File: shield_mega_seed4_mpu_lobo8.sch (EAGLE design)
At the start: 37 parts, among them U1 GY-521MPU6050

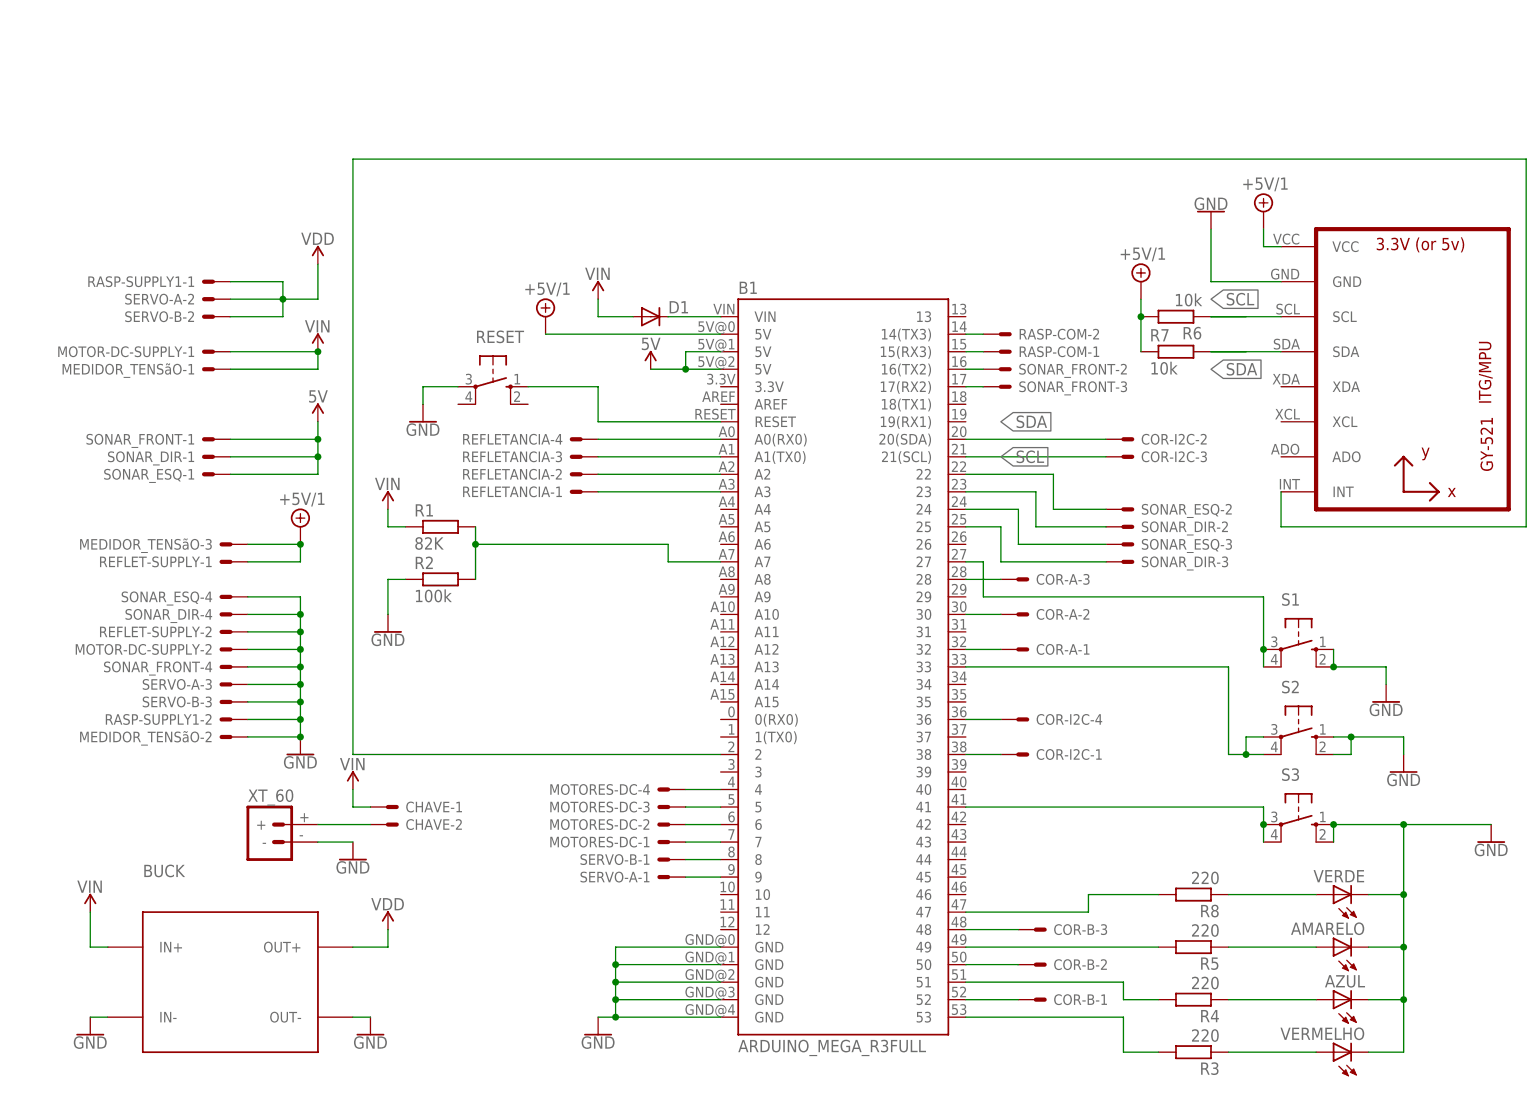
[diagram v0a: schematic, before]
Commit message: Adição de módulo bluetooth; Remoção do buck; Remoção de conector XT-60; Remoção de conector da chave;
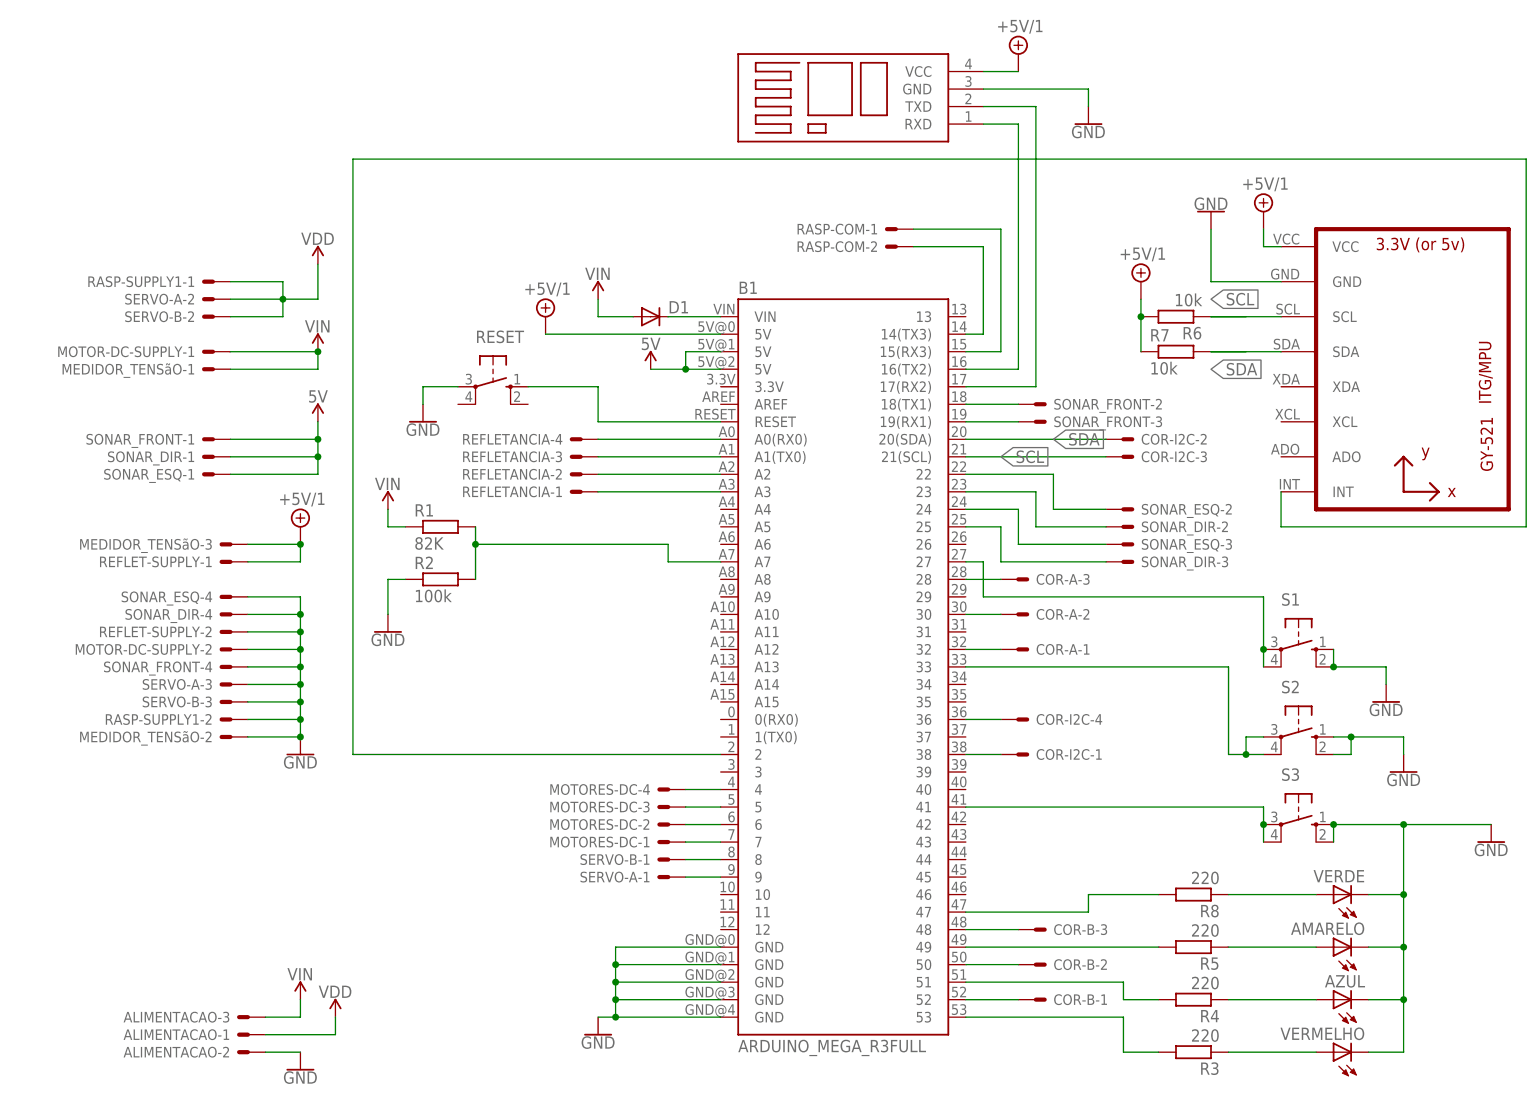
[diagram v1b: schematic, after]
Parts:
- removed BUCK: DC-DC-STEP-DOWN-LM2596, 1484249208697-powermodules:DC-DC-STEP-DOWN-LM2596
- removed CHAVE: 22-23-2021, con-molex:22-23-2021
- removed XT_60: (no value), Robotica-IFRN-SC-conectores:BATTERY_CONNXT60
- added ALIMENTACAO: 22-23-2031, con-molex:22-23-2031
- added B2: (no value), Bluetooth:BLUETOOTH
- R1, R2: device rcl:R-EU_0207/12 -> rcl:R-EU_0204/7
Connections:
- new net N$43: B1.17(RX2), B2.TXD
- net +5V/1: now also B2.VCC
- net GND: now also ALIMENTACAO-2.S, B2.GND; no longer BUCK.IN-, BUCK.OUT-, XT_60.-
- net N$11: now also B1.19(RX1), SONAR_FRONT-3.S; no longer B1.16(TX2), SONAR_FRONT-2.S
- net N$12: now also B1.18(TX1), SONAR_FRONT-2.S; no longer B1.17(RX2), SONAR_FRONT-3.S
- net N$13: now also B1.16(TX2), B2.RXD; no longer CHAVE-2.S, XT_60.+
- net VDD: now also ALIMENTACAO-1.S; no longer BUCK.OUT+
- net VIN: now also ALIMENTACAO-3.S; no longer BUCK.IN+, CHAVE-1.S
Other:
- moved on the sheet: RASP-COM-1, RASP-COM-2, SONAR_FRONT-2, SONAR_FRONT-3

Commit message: Remoção do conector do multímetro; remoção do conector de alimentação do sensor de refletância; remoção do conector de alimentação do motor;
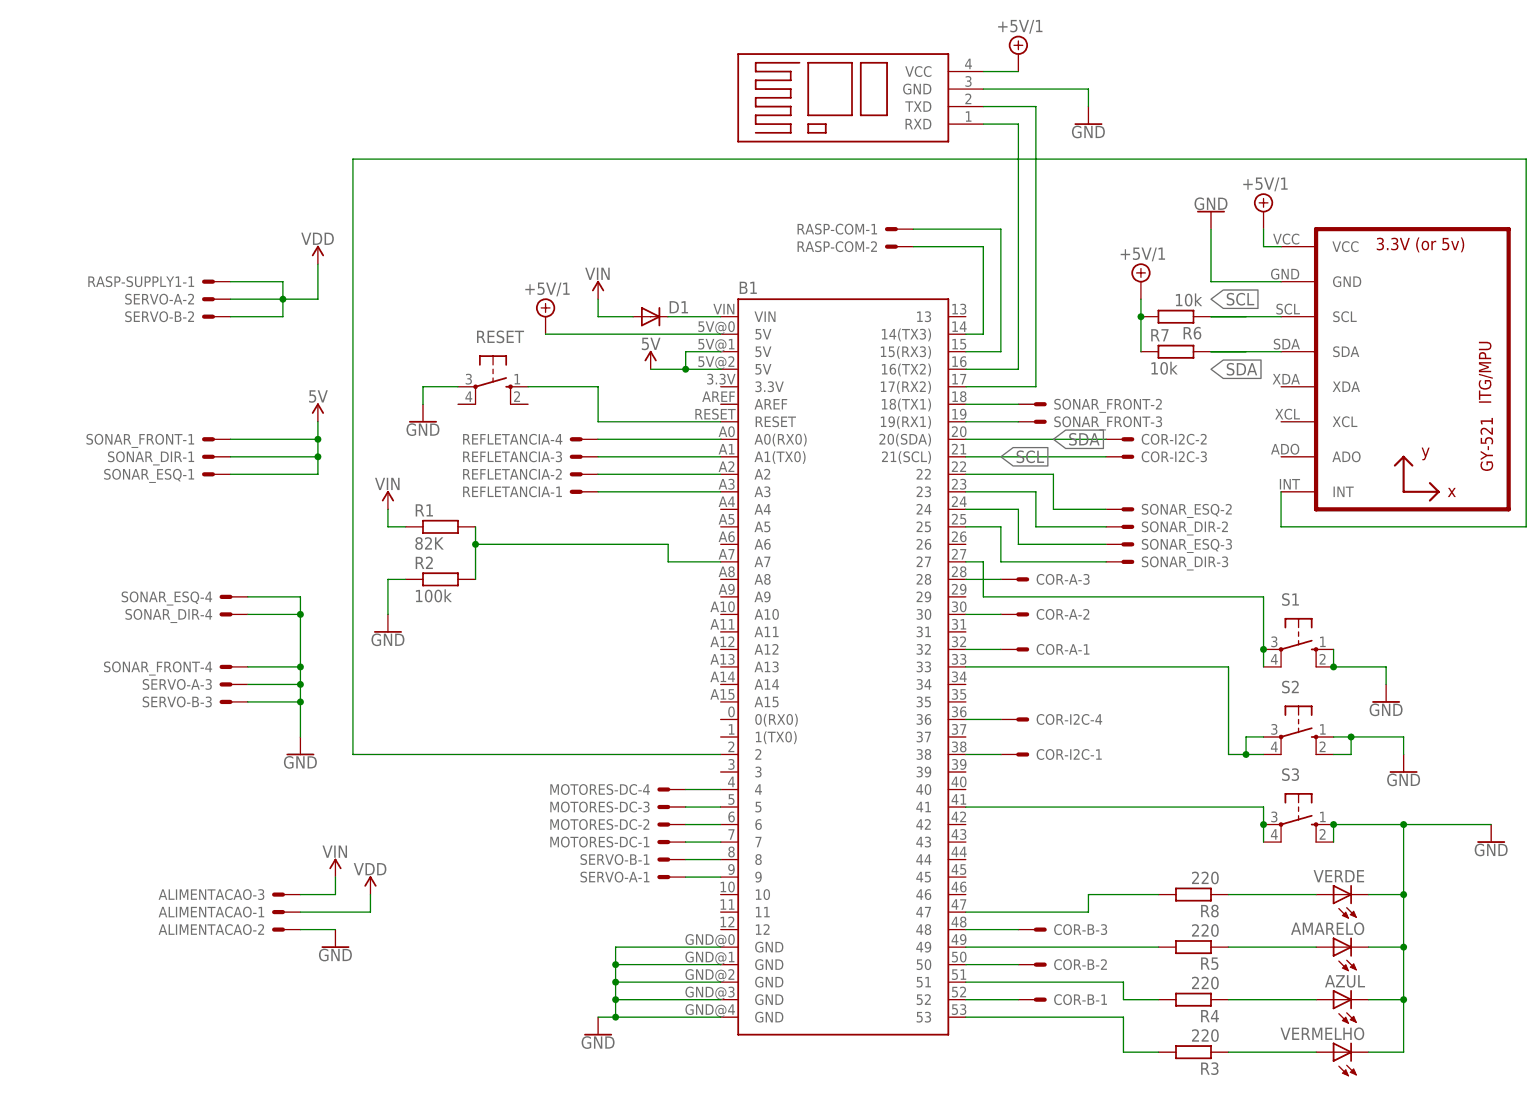
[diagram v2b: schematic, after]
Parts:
- removed MEDIDOR_TENSãO: 22-23-2031, con-molex:22-23-2031
- removed MOTOR-DC-SUPPLY, REFLET-SUPPLY: 22-23-2021, con-molex:22-23-2021
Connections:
- net +5V/1: no longer MEDIDOR_TENSãO-3.S, REFLET-SUPPLY-1.S
- net GND: no longer MEDIDOR_TENSãO-2.S, MOTOR-DC-SUPPLY-2.S, RASP-SUPPLY1-2.S, REFLET-SUPPLY-2.S
- net VIN: no longer MEDIDOR_TENSãO-1.S, MOTOR-DC-SUPPLY-1.S
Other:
- moved on the sheet: ALIMENTACAO-1, ALIMENTACAO-2, ALIMENTACAO-3
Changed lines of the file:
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@@
 </classes>
 <parts>
-<part name="B1" library="SparkFun-Boards3" deviceset="ARDUINO_MEGA_R3" device="FULL"/>
+<part name="B1" library="SparkFun-Boards3" deviceset="ARDUINO_MEGA_R3" device="FULL" value=""/>
 <part name="SUPPLY1" library="SparkFun-PowerSymbols" deviceset="VIN" device=""/>
 <part name="SUPPLY2" library="SparkFun-PowerSymbols" deviceset="VIN" device=""/>
@@
 <part name="SERVO-B" library="con-molex" deviceset="22-23-2031" device="" value=""/>
 <part name="MOTORES-DC" library="con-molex" deviceset="22-23-2041" device="" value=""/>
-<part name="MOTOR-DC-SUPPLY" library="con-molex" deviceset="22-23-2021" device="" value=""/>
 <part name="SUPPLY6" library="SparkFun-PowerSymbols" deviceset="VDD" device=""/>
 <part name="SUPPLY7" library="SparkFun-PowerSymbols" deviceset="VDD" device=""/>
@@
 <part name="RESET" library="switch-omron" deviceset="10-XX" device=""/>
 <part name="GND11" library="SparkFun-PowerSymbols" deviceset="GND" device=""/>
-<part name="MEDIDOR_TENSãO" library="con-molex" deviceset="22-23-2031" device="" value=""/>
-<part name="REFLET-SUPPLY" library="con-molex" deviceset="22-23-2021" device="" value=""/>
-<part name="SUPPLY4" library="SparkFun-PowerSymbols" deviceset="VIN" device=""/>
 <part name="SONAR_DIR" library="con-molex" deviceset="22-23-2041" device="" value=""/>
 <part name="SUPPLY9" library="SparkFun-PowerSymbols" deviceset="5V" device=""/>
 <part name="SONAR_ESQ" library="con-molex" deviceset="22-23-2041" device="" value=""/>
 <part name="SUPPLY10" library="supply2" deviceset="+5V/1" device=""/>
-<part name="SUPPLY11" library="supply2" deviceset="+5V/1" device=""/>
 <part name="U1" library="gy-521" deviceset="GY-521" device="MPU6050"/>
 <part name="GND12" library="SparkFun-PowerSymbols" deviceset="GND" device=""/>
@@
 <instances>
 <instance part="B1" gate="G$1" x="83.82" y="45.72"/>
-<instance part="SUPPLY1" gate="G$1" x="5.08" y="-2.54"/>
+<instance part="SUPPLY1" gate="G$1" x="10.16" y="15.24"/>
 <instance part="SUPPLY2" gate="G$1" x="48.26" y="99.06"/>
-<instance part="GND1" gate="1" x="5.08" y="-12.7"/>
+<instance part="GND1" gate="1" x="10.16" y="5.08"/>
 <instance part="GND2" gate="1" x="48.26" y="-7.62"/>
 <instance part="SONAR_FRONT" gate="-1" x="-7.62" y="78.74" rot="R180"/>
@@
 <instance part="MOTORES-DC" gate="-3" x="58.42" y="25.4" rot="R180"/>
 <instance part="MOTORES-DC" gate="-4" x="58.42" y="27.94" rot="R180"/>
-<instance part="MOTOR-DC-SUPPLY" gate="-1" x="-7.62" y="91.44" rot="R180"/>
-<instance part="MOTOR-DC-SUPPLY" gate="-2" x="-5.08" y="48.26" rot="R180"/>
-<instance part="SUPPLY6" gate="VDD" x="10.16" y="-5.08"/>
+<instance part="SUPPLY6" gate="VDD" x="15.24" y="12.7"/>
 <instance part="SUPPLY7" gate="VDD" x="7.62" y="104.14"/>
 <instance part="RASP-SUPPLY1" gate="-1" x="-7.62" y="101.6" rot="R180"/>
-<instance part="RASP-SUPPLY1" gate="-2" x="-5.08" y="38.1" rot="R180"/>
 <instance part="RASP-COM" gate="-1" x="91.44" y="109.22" rot="R180"/>
 <instance part="RASP-COM" gate="-2" x="91.44" y="106.68" rot="R180"/>
@@
 <instance part="RESET" gate="1" x="33.02" y="86.36" rot="R270"/>
 <instance part="GND11" gate="1" x="22.86" y="81.28"/>
-<instance part="MEDIDOR_TENSãO" gate="-1" x="-7.62" y="88.9" rot="R180"/>
-<instance part="MEDIDOR_TENSãO" gate="-2" x="-5.08" y="35.56" rot="R180"/>
-<instance part="MEDIDOR_TENSãO" gate="-3" x="-5.08" y="63.5" rot="R180"/>
-<instance part="REFLET-SUPPLY" gate="-1" x="-5.08" y="60.96" rot="R180"/>
-<instance part="REFLET-SUPPLY" gate="-2" x="-5.08" y="50.8" rot="R180"/>
-<instance part="SUPPLY4" gate="G$1" x="7.62" y="91.44"/>
 <instance part="SONAR_DIR" gate="-1" x="-7.62" y="76.2" rot="R180"/>
 <instance part="SONAR_DIR" gate="-2" x="124.46" y="66.04"/>
@@
 <instance part="SONAR_ESQ" gate="-4" x="-5.08" y="55.88" rot="R180"/>
 <instance part="SUPPLY10" gate="G$1" x="40.64" y="96.52"/>
-<instance part="SUPPLY11" gate="G$1" x="5.08" y="66.04"/>
 <instance part="U1" gate="G$1" x="162.56" y="91.44"/>
 <instance part="GND12" gate="1" x="137.16" y="111.76" rot="R180"/>
@@
 <instance part="VERDE" gate="G$1" x="154.94" y="12.7" rot="R90"/>
 <instance part="COR-I2C" gate="-4" x="109.22" y="38.1"/>
-<instance part="ALIMENTACAO" gate="-1" x="-2.54" y="-7.62" rot="R180"/>
-<instance part="ALIMENTACAO" gate="-2" x="-2.54" y="-10.16" rot="R180"/>
-<instance part="ALIMENTACAO" gate="-3" x="-2.54" y="-5.08" rot="R180"/>
+<instance part="ALIMENTACAO" gate="-1" x="2.54" y="10.16" rot="R180"/>
+<instance part="ALIMENTACAO" gate="-2" x="2.54" y="7.62" rot="R180"/>
+<instance part="ALIMENTACAO" gate="-3" x="2.54" y="12.7" rot="R180"/>
 <instance part="B2" gate="G$1" x="83.82" y="129.54" rot="R180"/>
 <instance part="SUPPLY5" gate="G$1" x="109.22" y="134.62"/>
@@
 <segment>
 <pinref part="GND1" gate="1" pin="GND"/>
-<wire x1="0" y1="-10.16" x2="5.08" y2="-10.16" width="0.1524" layer="91"/>
+<wire x1="5.08" y1="7.62" x2="10.16" y2="7.62" width="0.1524" layer="91"/>
 <pinref part="ALIMENTACAO" gate="-2" pin="S"/>
 </segment>
 <segment>
 <pinref part="GND3" gate="1" pin="GND"/>
-<wire x1="5.08" y1="35.56" x2="5.08" y2="38.1" width="0.1524" layer="91"/>
 <pinref part="SERVO-B" gate="-3" pin="S"/>
-<wire x1="5.08" y1="38.1" x2="5.08" y2="40.64" width="0.1524" layer="91"/>
+<wire x1="5.08" y1="35.56" x2="5.08" y2="40.64" width="0.1524" layer="91"/>
 <wire x1="5.08" y1="40.64" x2="-2.54" y2="40.64" width="0.1524" layer="91"/>
 <pinref part="SERVO-A" gate="-3" pin="S"/>
@@
 <wire x1="5.08" y1="45.72" x2="5.08" y2="43.18" width="0.1524" layer="91"/>
 <pinref part="SONAR_FRONT" gate="-4" pin="S"/>
-<wire x1="5.08" y1="50.8" x2="5.08" y2="48.26" width="0.1524" layer="91"/>
-<wire x1="5.08" y1="48.26" x2="5.08" y2="45.72" width="0.1524" layer="91"/>
+<wire x1="5.08" y1="53.34" x2="5.08" y2="45.72" width="0.1524" layer="91"/>
 <wire x1="-2.54" y1="45.72" x2="5.08" y2="45.72" width="0.1524" layer="91"/>
 <junction x="5.08" y="45.72"/>
-<pinref part="RASP-SUPPLY1" gate="-2" pin="S"/>
-<wire x1="-2.54" y1="38.1" x2="5.08" y2="38.1" width="0.1524" layer="91"/>
-<junction x="5.08" y="38.1"/>
-<pinref part="MEDIDOR_TENSãO" gate="-2" pin="S"/>
-<wire x1="-2.54" y1="35.56" x2="5.08" y2="35.56" width="0.1524" layer="91"/>
-<junction x="5.08" y="35.56"/>
-<pinref part="REFLET-SUPPLY" gate="-2" pin="S"/>
-<wire x1="-2.54" y1="50.8" x2="5.08" y2="50.8" width="0.1524" layer="91"/>
-<pinref part="MOTOR-DC-SUPPLY" gate="-2" pin="S"/>
-<wire x1="-2.54" y1="48.26" x2="5.08" y2="48.26" width="0.1524" layer="91"/>
-<junction x="5.08" y="48.26"/>
 <pinref part="SONAR_DIR" gate="-4" pin="S"/>
 <wire x1="-2.54" y1="53.34" x2="5.08" y2="53.34" width="0.1524" layer="91"/>
-<wire x1="5.08" y1="53.34" x2="5.08" y2="50.8" width="0.1524" layer="91"/>
-<junction x="5.08" y="50.8"/>
 <pinref part="SONAR_ESQ" gate="-4" pin="S"/>
 <wire x1="-2.54" y1="55.88" x2="5.08" y2="55.88" width="0.1524" layer="91"/>
@@
 <segment>
 <pinref part="SUPPLY1" gate="G$1" pin="VIN"/>
-<wire x1="5.08" y1="-5.08" x2="5.08" y2="-2.54" width="0.1524" layer="91"/>
+<wire x1="10.16" y1="12.7" x2="10.16" y2="15.24" width="0.1524" layer="91"/>
 <pinref part="ALIMENTACAO" gate="-3" pin="S"/>
-<wire x1="0" y1="-5.08" x2="5.08" y2="-5.08" width="0.1524" layer="91"/>
-</segment>
-<segment>
-<pinref part="MOTOR-DC-SUPPLY" gate="-1" pin="S"/>
-<pinref part="SUPPLY4" gate="G$1" pin="VIN"/>
-<wire x1="-5.08" y1="91.44" x2="7.62" y2="91.44" width="0.1524" layer="91"/>
-<pinref part="MEDIDOR_TENSãO" gate="-1" pin="S"/>
-<wire x1="-5.08" y1="88.9" x2="7.62" y2="88.9" width="0.1524" layer="91"/>
-<wire x1="7.62" y1="88.9" x2="7.62" y2="91.44" width="0.1524" layer="91"/>
-<junction x="7.62" y="91.44"/>
+<wire x1="5.08" y1="12.7" x2="10.16" y2="12.7" width="0.1524" layer="91"/>
 </segment>
 </net>
@@
 <pinref part="ALIMENTACAO" gate="-1" pin="S"/>
 <pinref part="SUPPLY6" gate="VDD" pin="VDD"/>
-<wire x1="0" y1="-7.62" x2="10.16" y2="-7.62" width="0.1524" layer="91"/>
-<wire x1="10.16" y1="-7.62" x2="10.16" y2="-5.08" width="0.1524" layer="91"/>
+<wire x1="5.08" y1="10.16" x2="15.24" y2="10.16" width="0.1524" layer="91"/>
+<wire x1="15.24" y1="10.16" x2="15.24" y2="12.7" width="0.1524" layer="91"/>
 </segment>
 </net>
@@
 </segment>
 <segment>
-<pinref part="MEDIDOR_TENSãO" gate="-3" pin="S"/>
-<pinref part="SUPPLY11" gate="G$1" pin="+5V/1"/>
-<wire x1="-2.54" y1="63.5" x2="5.08" y2="63.5" width="0.1524" layer="91"/>
-<pinref part="REFLET-SUPPLY" gate="-1" pin="S"/>
-<wire x1="-2.54" y1="60.96" x2="5.08" y2="60.96" width="0.1524" layer="91"/>
-<wire x1="5.08" y1="60.96" x2="5.08" y2="63.5" width="0.1524" layer="91"/>
-<junction x="5.08" y="63.5"/>
-</segment>
-<segment>

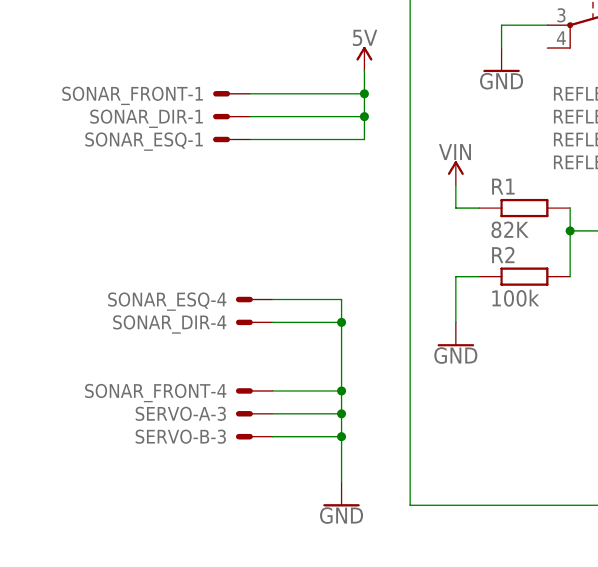
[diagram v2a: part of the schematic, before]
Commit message: remoção de erro que deixou o conector de alimentação sem terra
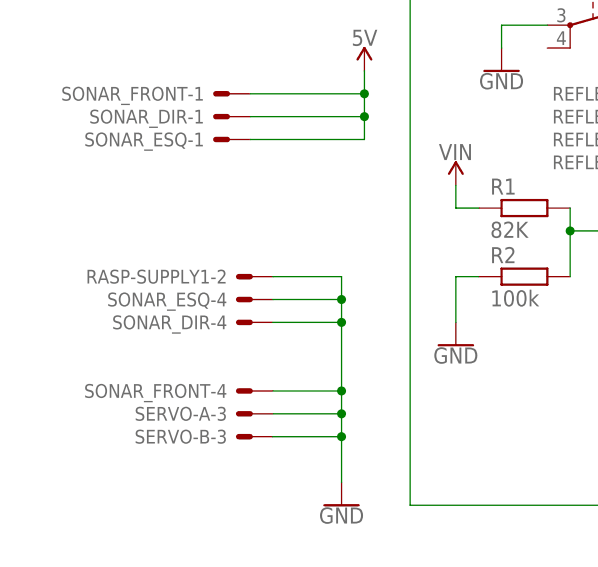
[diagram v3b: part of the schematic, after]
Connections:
- net GND: now also RASP-SUPPLY1-2.S
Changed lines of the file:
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@@
 <instance part="SUPPLY5" gate="G$1" x="109.22" y="134.62"/>
 <instance part="GND4" gate="1" x="119.38" y="124.46"/>
+<instance part="RASP-SUPPLY1" gate="-2" x="-5.08" y="58.42" rot="R180"/>
 </instances>
 <busses>
@@
 <wire x1="5.08" y1="55.88" x2="5.08" y2="53.34" width="0.1524" layer="91"/>
 <junction x="5.08" y="53.34"/>
+<pinref part="RASP-SUPPLY1" gate="-2" pin="S"/>
+<wire x1="-2.54" y1="58.42" x2="5.08" y2="58.42" width="0.1524" layer="91"/>
+<wire x1="5.08" y1="58.42" x2="5.08" y2="55.88" width="0.1524" layer="91"/>
+<junction x="5.08" y="55.88"/>
 </segment>
 <segment>
